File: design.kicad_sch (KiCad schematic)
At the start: 80 parts, among them J1 2601-3108, J10 Conn_01x04, J11 Conn_01x04, J12 Conn_01x03, J13 Conn_01x03, J14 Conn_01x04, J2 2601-3108, J3 2601-3108, J4 TYPE-C-31-M-12, J5 SKEDD-UPDI-4, J6 Conn_01x04, J7 Conn_01x04, J8 Conn_01x04, J9 Conn_01x04, U1 ATtiny1616-S, U2 AP2112K-3.3, U3 CP2105

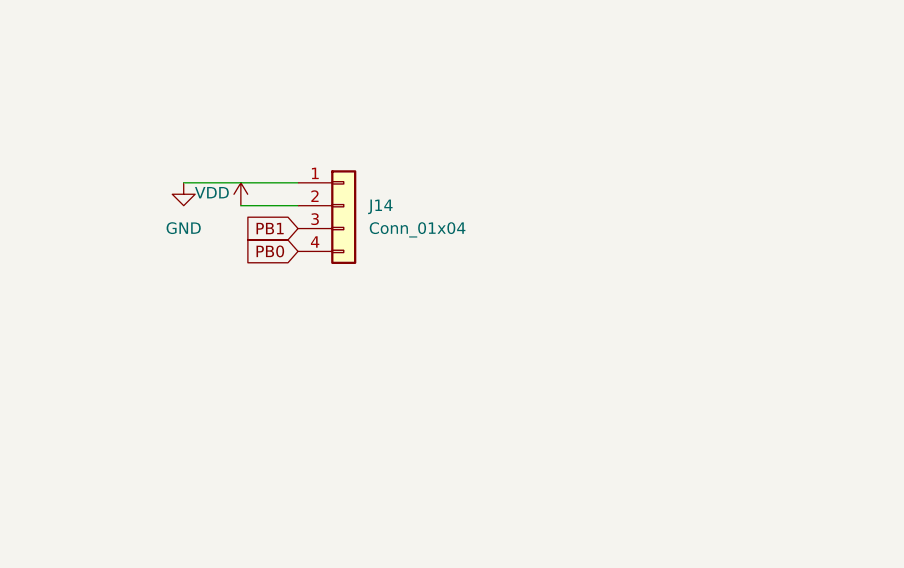
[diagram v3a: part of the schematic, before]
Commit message: change to BM04B-SRSS-TB symbol
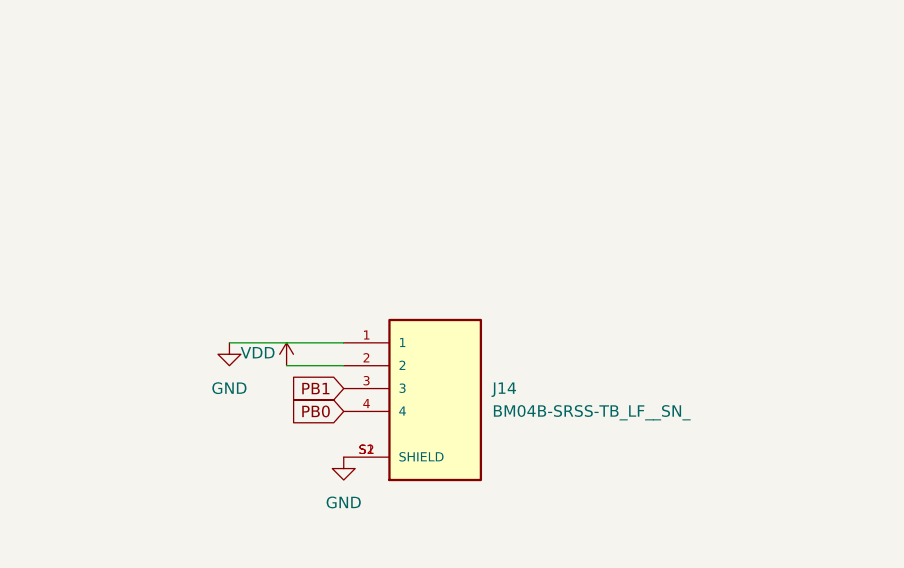
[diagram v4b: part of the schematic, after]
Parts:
- removed J14: Conn_01x04, Snapeda:BM04B-SRSS-TB_LF__SN__JST_BM04B-SRSS-TB_LF__SN_, symbol Connector_Generic:Conn_01x04
- added J14: BM04B-SRSS-TB_LF__SN_, Snapeda:BM04B-SRSS-TB_LF__SN__JST_BM04B-SRSS-TB_LF__SN_, symbol Snapeda:BM04B-SRSS-TB_LF__SN_
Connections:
- net GND: now also J14.1, J14.S1 (SHIELD), J14.S2 (SHIELD)
- net PB0: now also J14.4
- net PB1: now also J14.3
- net VDD: now also J14.2
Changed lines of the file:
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@@
     (stroke (width 0) (type default) (color 0 0 0 0))
   )
-  (wire (pts (xy 53.34 226.06) (xy 66.04 226.06))
+  (wire (pts (xy 58.42 243.84) (xy 71.12 243.84))
     (stroke (width 0) (type default) (color 0 0 0 0))
   )
@@
     (stroke (width 0) (type default) (color 0 0 0 0))
   )
-  (wire (pts (xy 59.69 228.6) (xy 66.04 228.6))
+  (wire (pts (xy 64.77 246.38) (xy 71.12 246.38))
     (stroke (width 0) (type default) (color 0 0 0 0))
   )
@@
     )
   )
-  (global_label "PB1" (shape input) (at 66.04 231.14 180) (fields_autoplaced)
+  (global_label "PB1" (shape input) (at 71.12 248.92 180) (fields_autoplaced)
     (effects (font (size 1.27 1.27)) (justify right))
-    (property "Referenzen zwischen Schaltplänen" "${INTERSHEET_REFS}" (id 0) (at 59.9663 231.0606 0)
+    (property "Referenzen zwischen Schaltplänen" "${INTERSHEET_REFS}" (id 0) (at 65.0463 248.8406 0)
       (effects (font (size 1.27 1.27)) (justify right) hide)
     )
@@
     )
   )
-  (global_label "PB0" (shape input) (at 66.04 233.68 180) (fields_autoplaced)
+  (global_label "PB0" (shape input) (at 71.12 251.46 180) (fields_autoplaced)
     (effects (font (size 1.27 1.27)) (justify right))
-    (property "Referenzen zwischen Schaltplänen" "${INTERSHEET_REFS}" (id 0) (at 59.9663 233.6006 0)
+    (property "Referenzen zwischen Schaltplänen" "${INTERSHEET_REFS}" (id 0) (at 65.0463 251.3806 0)
       (effects (font (size 1.27 1.27)) (justify right) hide)
     )
@@
     (pin "1")
   )
+  (symbol (lib_id "Snapeda:BM04B-SRSS-TB_LF__SN_") (at 81.28 251.46 0) (unit 1)
+    (in_bom yes) (on_board yes) (fields_autoplaced)
+    (property "Reference" "J14" (id 0) (at 87.63 248.9199 0)
+      (effects (font (size 1.27 1.27)) (justify left))
+    )
+    (property "Value" "BM04B-SRSS-TB_LF__SN_" (id 1) (at 87.63 251.4599 0)
+      (effects (font (size 1.27 1.27)) (justify left))
+    )
+    (property "Footprint" "Snapeda:BM04B-SRSS-TB_LF__SN__JST_BM04B-SRSS-TB_LF__SN_" (id 2) (at 81.28 251.46 0)
+      (effects (font (size 1.27 1.27)) (justify bottom) hide)
+    )
+    (property "Datasheet" "" (id 3) (at 81.28 251.46 0)
+      (effects (font (size 1.27 1.27)) hide)
+    )
+    (property "MF" "JST Sales" (id 4) (at 81.28 251.46 0)
+      (effects (font (size 1.27 1.27)) (justify bottom) hide)
+    )
+    (property "MAXIMUM_PACKAGE_HEIGHT" "6.3 mm" (id 5) (at 81.28 251.46 0)
+      (effects (font (size 1.27 1.27)) (justify bottom) hide)
+    )
+    (property "Package" "None" (id 6) (at 81.28 251.46 0)
+      (effects (font (size 1.27 1.27)) (justify bottom) hide)
+    )
+    (property "Price" "None" (id 7) (at 81.28 251.46 0)
+      (effects (font (size 1.27 1.27)) (justify bottom) hide)
+    )
+    (property "Check_prices" "https://www.snapeda.com/parts/BM04B-SRSS-TB(LF)(SN)/JST+Sales+America+Inc./view-part/?ref=eda" (id 8) (at 81.28 251.46 0)
+      (effects (font (size 1.27 1.27)) (justify bottom) hide)
+    )
+    (property "STANDARD" "Manufacturer Recommendations" (id 9) (at 81.28 251.46 0)
+      (effects (font (size 1.27 1.27)) (justify bottom) hide)
+    )
+    (property "PARTREV" "N/A" (id 10) (at 81.28 251.46 0)
+      (effects (font (size 1.27 1.27)) (justify bottom) hide)
+    )
+    (property "SnapEDA_Link" "https://www.snapeda.com/parts/BM04B-SRSS-TB(LF)(SN)/JST+Sales+America+Inc./view-part/?ref=snap" (id 11) (at 81.28 251.46 0)
+      (effects (font (size 1.27 1.27)) (justify bottom) hide)
+    )
+    (property "MP" "BM04B-SRSS-TB(LF)(SN)" (id 12) (at 81.28 251.46 0)
+      (effects (font (size 1.27 1.27)) (justify bottom) hide)
+    )
+    (property "Description" "\n                        \n                            Connector Header Surface Mount 4 position 0.039 (1.00mm)\n                        \n" (id 13) (at 81.28 251.46 0)
+      (effects (font (size 1.27 1.27)) (justify bottom) hide)
+    )
+    (property "MANUFACTURER" "JST Sales America Inc." (id 14) (at 81.28 251.46 0)
+      (effects (font (size 1.27 1.27)) (justify bottom) hide)
+    )
+    (property "Availability" "In Stock" (id 15) (at 81.28 251.46 0)
+      (effects (font (size 1.27 1.27)) (justify bottom) hide)
+    )
+    (property "SNAPEDA_PN" "BM04B-SRSS-TB(LF)(SN)" (id 16) (at 81.28 251.46 0)
+      (effects (font (size 1.27 1.27)) (justify bottom) hide)
+    )
+    (pin "1")
+    (pin "2")
+    (pin "3")
+    (pin "4")
+    (pin "S1")
+    (pin "S2")
+  )
   (symbol (lib_id "power:GND") (at 388.62 48.26 0) (unit 1)
     (in_bom yes) (on_board yes) (fields_autoplaced)
@@
     (pin "1")
   )
-  (symbol (lib_id "power:VDD") (at 59.69 228.6 0) (mirror y) (unit 1)
+  (symbol (lib_id "power:VDD") (at 64.77 246.38 0) (mirror y) (unit 1)
     (in_bom yes) (on_board yes)
-    (property "Reference" "#PWR0185" (id 0) (at 59.69 232.41 0)
+    (property "Reference" "#PWR0185" (id 0) (at 64.77 250.19 0)
       (effects (font (size 1.27 1.27)) hide)
     )
-    (property "Value" "VDD" (id 1) (at 56.515 227.203 0))
-    (property "Footprint" "" (id 2) (at 59.69 228.6 0)
+    (property "Value" "VDD" (id 1) (at 61.595 244.983 0))
+    (property "Footprint" "" (id 2) (at 64.77 246.38 0)
       (effects (font (size 1.27 1.27)) hide)
     )
-    (property "Datasheet" "" (id 3) (at 59.69 228.6 0)
+    (property "Datasheet" "" (id 3) (at 64.77 246.38 0)
       (effects (font (size 1.27 1.27)) hide)
     )
@@
     (pin "1")
   )
+  (symbol (lib_id "power:GND") (at 71.12 256.54 0) (unit 1)
+    (in_bom yes) (on_board yes) (fields_autoplaced)
+    (property "Reference" "#PWR?" (id 0) (at 71.12 262.89 0)
+      (effects (font (size 1.27 1.27)) hide)
+    )
+    (property "Value" "GND" (id 1) (at 71.12 261.62 0))
+    (property "Footprint" "" (id 2) (at 71.12 256.54 0)
+      (effects (font (size 1.27 1.27)) hide)
+    )
+    (property "Datasheet" "" (id 3) (at 71.12 256.54 0)
+      (effects (font (size 1.27 1.27)) hide)
+    )
+    (pin "1")
+  )
   (symbol (lib_id "power:VDD") (at 355.6 185.42 0) (mirror y) (unit 1)
     (in_bom yes) (on_board yes)
@@
     (pin "1")
   )
-  (symbol (lib_id "Connector_Generic:Conn_01x04") (at 71.12 228.6 0) (unit 1)
-    (in_bom yes) (on_board yes) (fields_autoplaced)
-    (property "Reference" "J14" (id 0) (at 73.914 228.5999 0)
-      (effects (font (size 1.27 1.27)) (justify left))
-    )
-    (property "Value" "Conn_01x04" (id 1) (at 73.914 231.1399 0)
-      (effects (font (size 1.27 1.27)) (justify left))
-    )
-    (property "Footprint" "Snapeda:BM04B-SRSS-TB_LF__SN__JST_BM04B-SRSS-TB_LF__SN_" (id 2) (at 71.12 228.6 0)
-      (effects (font (size 1.27 1.27)) hide)
-    )
-    (property "Datasheet" "~" (id 3) (at 71.12 228.6 0)
-      (effects (font (size 1.27 1.27)) hide)
-    )
-    (pin "1")
-    (pin "2")
-    (pin "3")
-    (pin "4")
-  )
   (symbol (lib_id "power:VDD") (at 167.005 132.08 0) (mirror y) (unit 1)
     (in_bom yes) (on_board yes)
@@
     (pin "4")
   )
-  (symbol (lib_id "power:GND") (at 53.34 226.06 0) (unit 1)
+  (symbol (lib_id "power:GND") (at 58.42 243.84 0) (unit 1)
     (in_bom yes) (on_board yes) (fields_autoplaced)
-    (property "Reference" "#PWR0186" (id 0) (at 53.34 232.41 0)
+    (property "Reference" "#PWR0186" (id 0) (at 58.42 250.19 0)
       (effects (font (size 1.27 1.27)) hide)
     )
-    (property "Value" "GND" (id 1) (at 53.34 231.14 0))
-    (property "Footprint" "" (id 2) (at 53.34 226.06 0)
+    (property "Value" "GND" (id 1) (at 58.42 248.92 0))
+    (property "Footprint" "" (id 2) (at 58.42 243.84 0)
       (effects (font (size 1.27 1.27)) hide)
     )
-    (property "Datasheet" "" (id 3) (at 53.34 226.06 0)
+    (property "Datasheet" "" (id 3) (at 58.42 243.84 0)
       (effects (font (size 1.27 1.27)) hide)
     )
@@
       (reference "#PWR0188") (unit 1) (value "GND") (footprint "")
     )
+    (path "/3b010638-00df-47c0-8bf4-5465e4ce7746"
+      (reference "#PWR?") (unit 1) (value "GND") (footprint "")
+    )
     (path "/5005112b-a25c-4019-a0f7-bec67dd371e4"
       (reference "C1") (unit 1) (value "1uF") (footprint "Capacitor_SMD:C_0805_2012Metric")
@@
       (reference "J13") (unit 1) (value "Conn_01x03") (footprint "Connector_PinHeader_2.54mm:PinHeader_1x03_P2.54mm_Vertical")
     )
-    (path "/4817ef38-9f5b-45ae-8765-24c855bfece7"
-      (reference "J14") (unit 1) (value "Conn_01x04") (footprint "Snapeda:BM04B-SRSS-TB_LF__SN__JST_BM04B-SRSS-TB_LF__SN_")
+    (path "/1fb34454-9630-4e20-ab38-f23101dfc194"
+      (reference "J14") (unit 1) (value "BM04B-SRSS-TB_LF__SN_") (footprint "Snapeda:BM04B-SRSS-TB_LF__SN__JST_BM04B-SRSS-TB_LF__SN_")
     )
     (path "/911d639f-09b2-4116-af1e-a088e2cc31e7"
